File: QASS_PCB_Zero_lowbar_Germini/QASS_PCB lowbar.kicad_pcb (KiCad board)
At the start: 2 copper layers, 219.1 x 110.5 mm, 108 parts, among them J2 Conn_01x05_Pin, J3 Conn_01x05_Pin, J4 Conn_01x02_Pin, J5 Conn_01x05_Pin, J6 Conn_01x05_Pin, U2 RP2040-Matrix

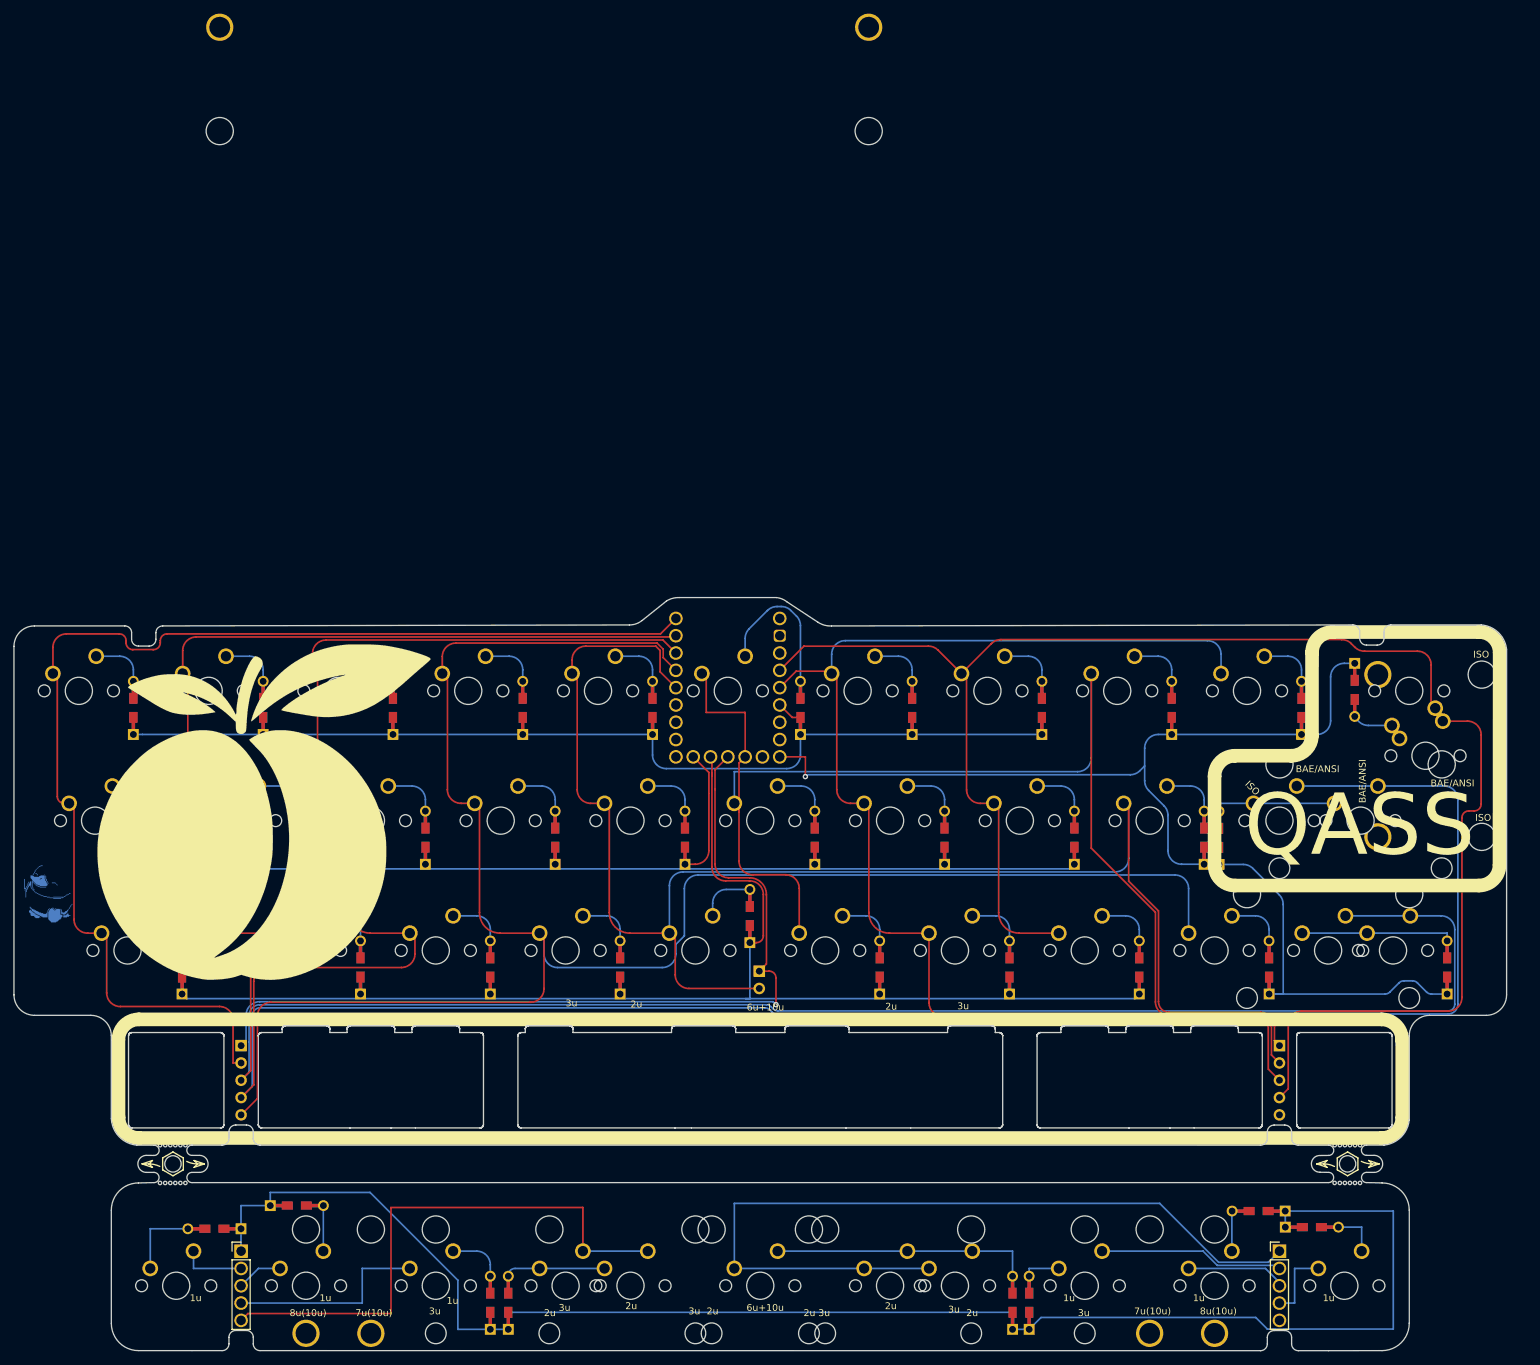
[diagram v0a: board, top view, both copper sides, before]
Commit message: v1.3 - silkscreen better and one diode orientation more consistent
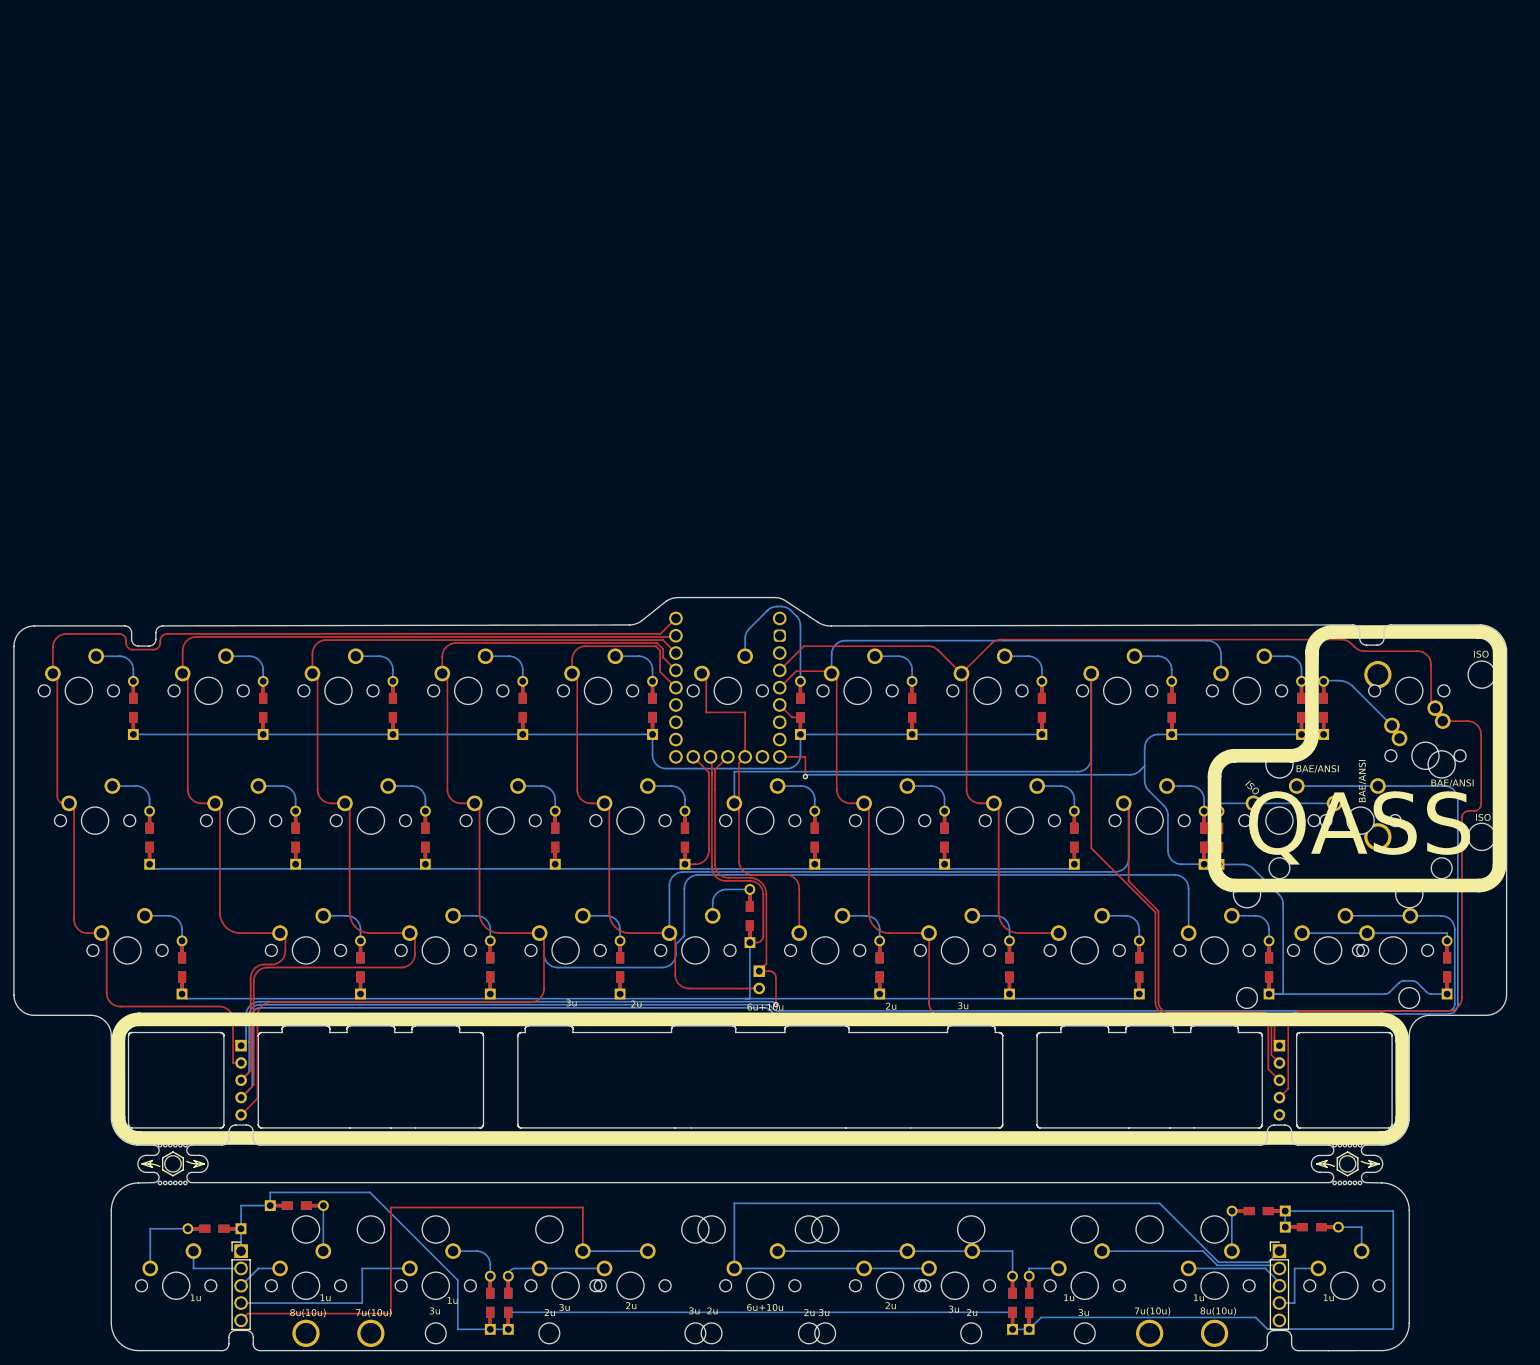
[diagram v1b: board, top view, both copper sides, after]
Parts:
- removed REF**: Clacktales_9mm_whiteSilk, Silkscreen:Clacktales_9mm_whiteSilk
- removed the Ref** at (60.8, 47.6)
- removed the Ref** at (109.0, 125.5)
- removed the Ref** at (206.4, 125.5)
- removed the Ref** at (157.9, 125.5)
- removed the Ref** at (60.4, 125.5)
- removed the Ref** at (29.5, 70.3)
- removed S6: MX_stab, PCM_marbastlib-mx:STAB_MX_P_6u
- added Ref**: Val**, Silkscreen:starpattern, B.Cu at (105.1, 121.7)
- added Ref**: Val**, Silkscreen:starpattern, B.Cu at (56.3, 124.2)
- added Ref**: Val**, Silkscreen:starpattern, B.Cu at (154.1, 126.3)
- added Ref**: Val**, Silkscreen:starpattern, B.Cu at (203.6, 122.0)
- D1, D10, D11, D12, D13, D14, D15, D16, D17, D18, D19, D2, D20, D21, D22, D23, D24, D25, D26, D27, D28, D29, D3, D30, D31, D32, D33, D34, D35, D36, D37, D38, D39, D4, D5, D6, D7, D8, D9: footprint footprints:Diode-dual -> TFL:Diode-dual
- moved D29 5.27 mm to (216.0, 32.3), turned to -90 degrees
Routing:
- net r4: track 177.2 -> 164.1 mm
- net Net-(D29-A): track 10.6 -> 15.0 mm
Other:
- board text added: "Re-fork of fork by quark-works: https://github.com/quark-works/QASS-Zero - v.1.3"
- board text removed: "Re-fork of fork by quark-works: https://github.com/quark-works/QASS-Zero"
